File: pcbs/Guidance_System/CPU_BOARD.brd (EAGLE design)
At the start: 100 x 52.1 mm, 33 parts, among them J1 22-27-2081-08, J10 22-27-2081-08, J11 22-27-2081-08, J12 22-27-2081-08, J13 22-27-2081-08, J14 22-27-2081-08, J15 22-27-2041-04, J16 22-27-2041-04, J17 22-27-2021-02, J2 22-27-2021-02, J3 22-27-2041-04, J4 22-27-2041-04, J5 22-27-2081-08, J6 22-27-2021-02, J7 22-27-2081-08, J8 22-27-2021-02, J9 22-27-2021-02

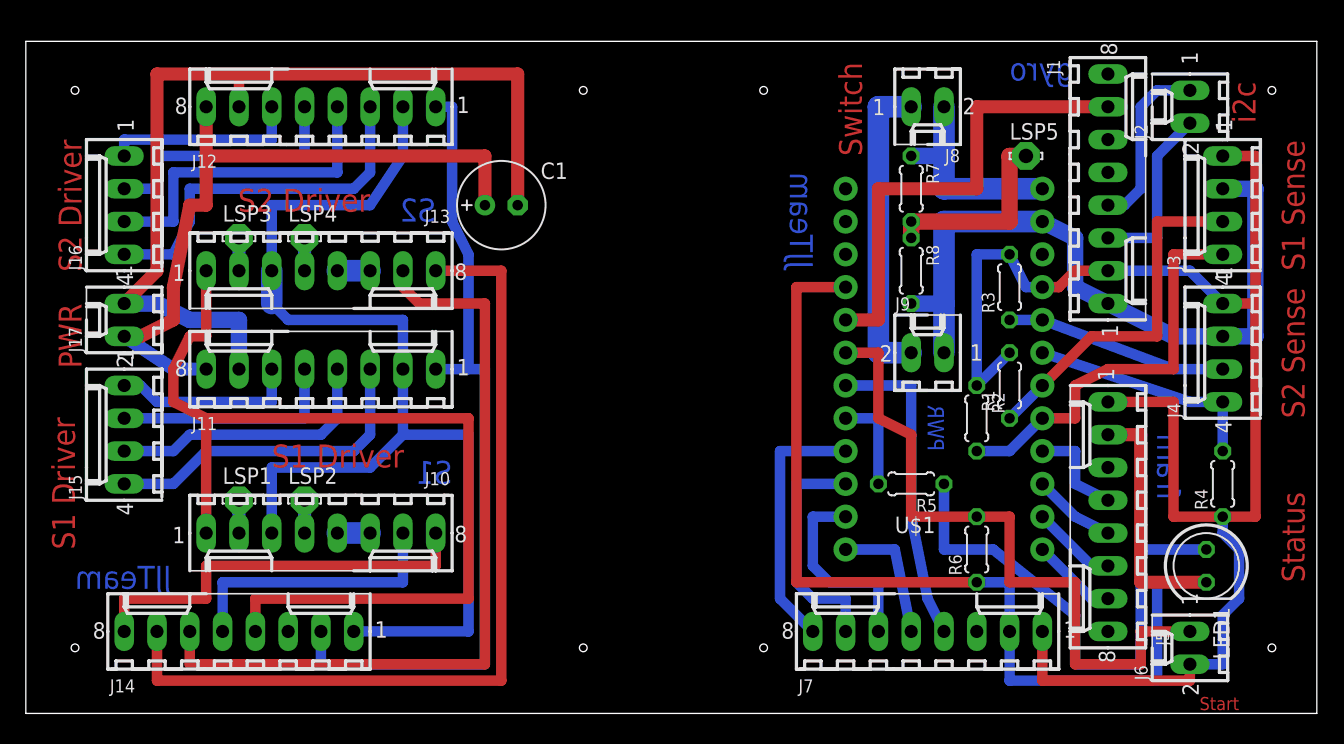
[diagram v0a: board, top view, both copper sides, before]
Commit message: * Moving 4-way connectors further apart, so housing will fit!
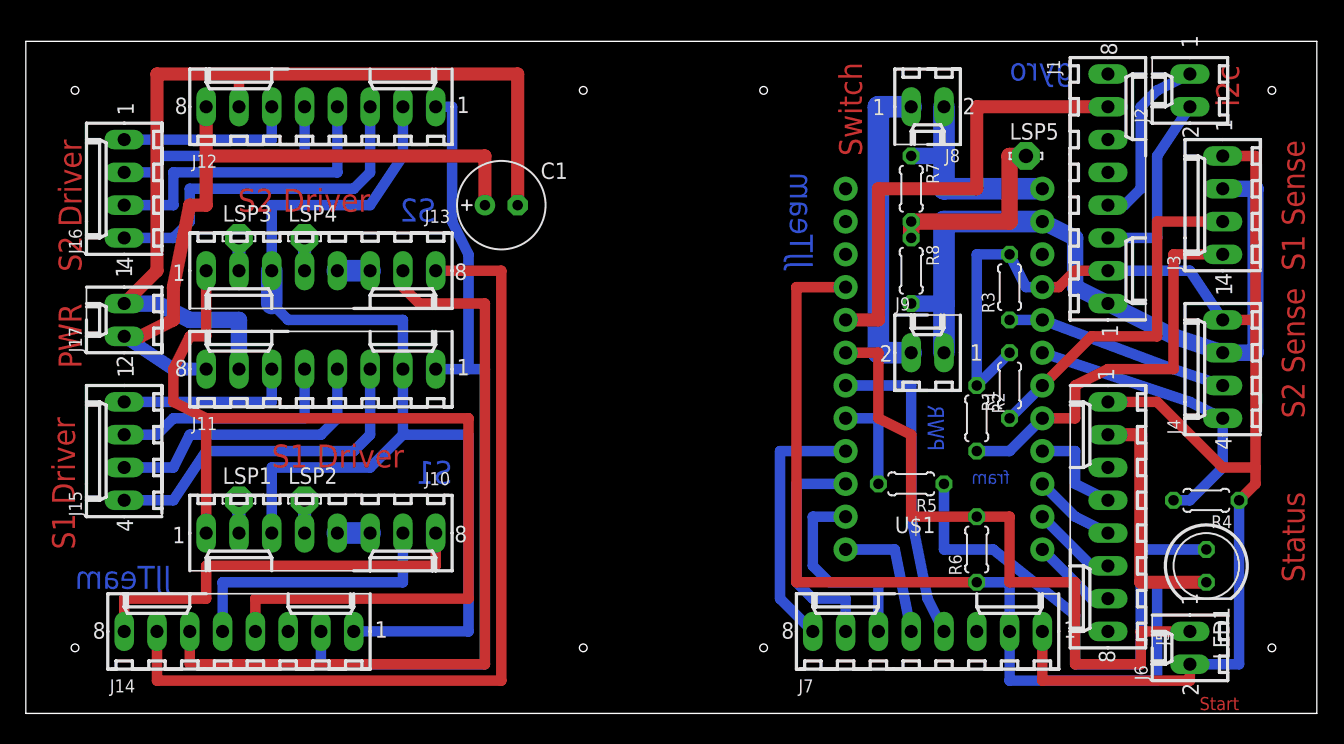
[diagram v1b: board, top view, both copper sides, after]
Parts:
- moved R4 1.80 mm to (91.4, 41.9), turned to 180 degrees
- moved J16 1.27 mm to (7.62, 66.0)
- moved J15 1.27 mm to (7.62, 45.7)
- moved J4 1.27 mm to (92.7, 52.1)
- moved J2 1.27 mm to (90.2, 73.7)
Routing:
- net N$10: track 18.4 -> 23.6 mm
- net N$3: track 120.8 -> 115.8 mm
- net N$24: track 55.8 -> 57.3 mm
- net N$43: track 25.4 -> 24.1 mm
- net N$42: track 20.3 -> 19.0 mm
- net N$41: track 15.2 -> 14.0 mm
- net N$44: track 28.8 -> 27.7 mm
- net N$39: track 21.4 -> 22.4 mm
- net N$40: track 25.7 -> 26.7 mm
- net N$1: track 13.8 -> 14.7 mm
- net N$38: track 17.8 -> 18.3 mm
- net N$37: track 14.5 -> 14.0 mm

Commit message: * Move connectors even further apart...just to to be safe.
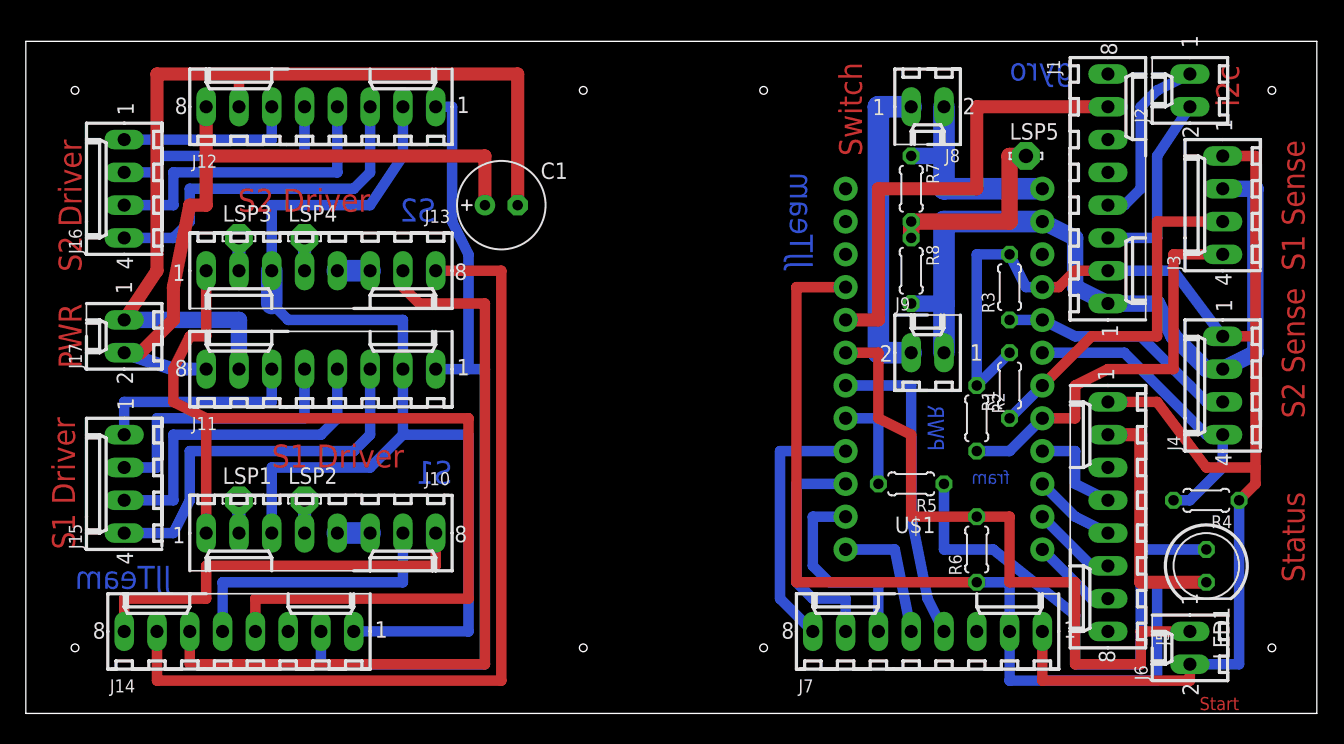
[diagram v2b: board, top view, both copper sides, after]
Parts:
- moved J15 2.54 mm to (7.62, 43.2)
- moved J17 1.27 mm to (7.62, 54.6)
- moved J4 1.27 mm to (92.7, 50.8)
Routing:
- net N$39: track 22.4 -> 25.9 mm
- net N$40: track 26.7 -> 30.0 mm
- net N$38: track 18.3 -> 21.6 mm
- net N$37: track 14.0 -> 16.5 mm
- net N$24: track 57.3 -> 59.4 mm
- net N$9: track 17.4 -> 18.9 mm
- net N$3: track 115.8 -> 116.7 mm
- net N$34: track 72.5 -> 73.2 mm

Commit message: * Fixed Track
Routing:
- net N$24: track 59.4 -> 60.4 mm
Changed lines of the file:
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@@
 <grid distance="0.05" unitdist="inch" unit="inch" style="lines" multiple="1" display="no" altdistance="0.025" altunitdist="inch" altunit="inch"/>
 <layers>
-<layer number="1" name="Top" color="4" fill="1" visible="yes" active="yes"/>
-<layer number="16" name="Bottom" color="1" fill="1" visible="no" active="yes"/>
+<layer number="1" name="Top" color="4" fill="1" visible="no" active="yes"/>
+<layer number="16" name="Bottom" color="1" fill="1" visible="yes" active="yes"/>
 <layer number="17" name="Pads" color="2" fill="1" visible="yes" active="yes"/>
 <layer number="18" name="Vias" color="2" fill="1" visible="yes" active="yes"/>
@@
 <contactref element="R3" pad="1"/>
 <wire x1="92.71" y1="49.53" x2="91.44" y2="49.53" width="0.8128" layer="16"/>
-<wire x1="91.44" y1="49.53" x2="90.17" y2="50.8" width="0.8128" layer="16"/>
-<wire x1="90.17" y1="50.8" x2="86.36" y2="54.61" width="0.8128" layer="16"/>
+<wire x1="91.44" y1="49.53" x2="86.36" y2="54.61" width="0.8128" layer="16"/>
 <wire x1="86.36" y1="54.61" x2="81.28" y2="54.61" width="0.8128" layer="16"/>
 <wire x1="81.28" y1="54.61" x2="78.74" y2="55.88" width="0.8128" layer="16"/>
@@
 <contactref element="J3" pad="2"/>
 <wire x1="92.71" y1="66.04" x2="95.25" y2="66.04" width="1.27" layer="16"/>
-<wire x1="95.25" y1="66.04" x2="95.25" y2="53.34" width="1.27" layer="16"/>
-<wire x1="95.25" y1="53.34" x2="92.71" y2="52.07" width="1.27" layer="16"/>
+<wire x1="95.25" y1="66.04" x2="95.25" y2="52.07" width="1.27" layer="16"/>
+<wire x1="95.25" y1="52.07" x2="92.71" y2="52.07" width="1.27" layer="16"/>
 <wire x1="92.71" y1="52.07" x2="91.44" y2="52.07" width="1.27" layer="16"/>
 <wire x1="91.44" y1="52.07" x2="88.9" y2="54.61" width="1.27" layer="16"/>
